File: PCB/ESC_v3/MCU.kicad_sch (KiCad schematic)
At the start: 44 parts, among them J10 Conn_01x01_Pin, J3 Conn_01x01_Pin, J4 Conn_01x01_Pin, J5 Conn_01x01_Pin, J6 Conn_01x01_Pin, J7 Conn_01x01_Pin, J8 Conn_01x01_Pin, J9 Conn_01x01_Pin, U5 STM32G431CBT6, Y2 24MHz

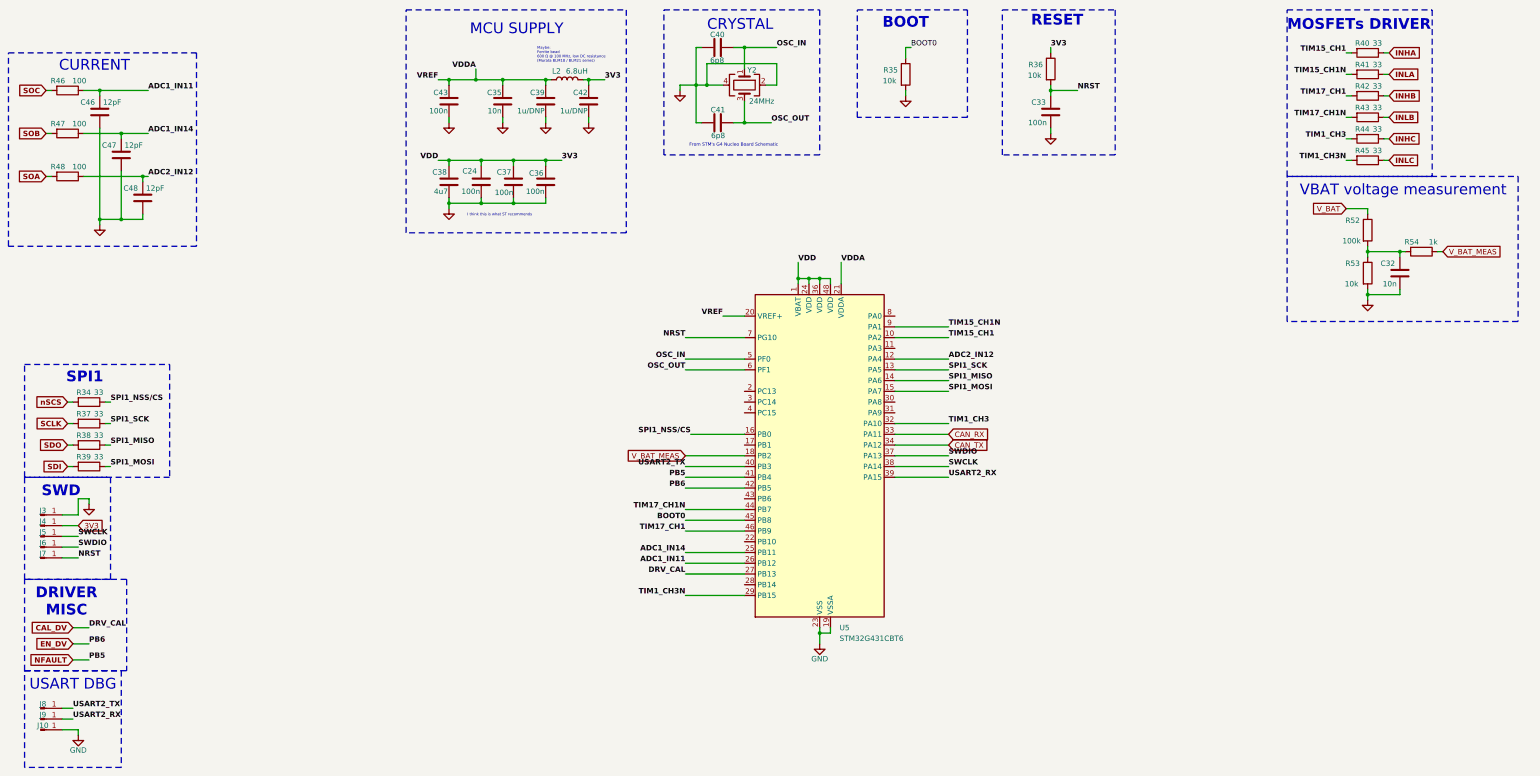
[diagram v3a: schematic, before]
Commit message: Reposition DRVR schematic elements
Adjust layout in PCB/ESC_v3/DRVR.kicad_sch: updated coordinates for rectangles, text labels, junctions, wires and pins to tidy and realign the driver schematic. Changes are graphical/coordinate-only (no netlist/electrical changes). Also touched project files (ESC_v3.*) and refreshed backup archives (deleted several older backups and added new snapshots).
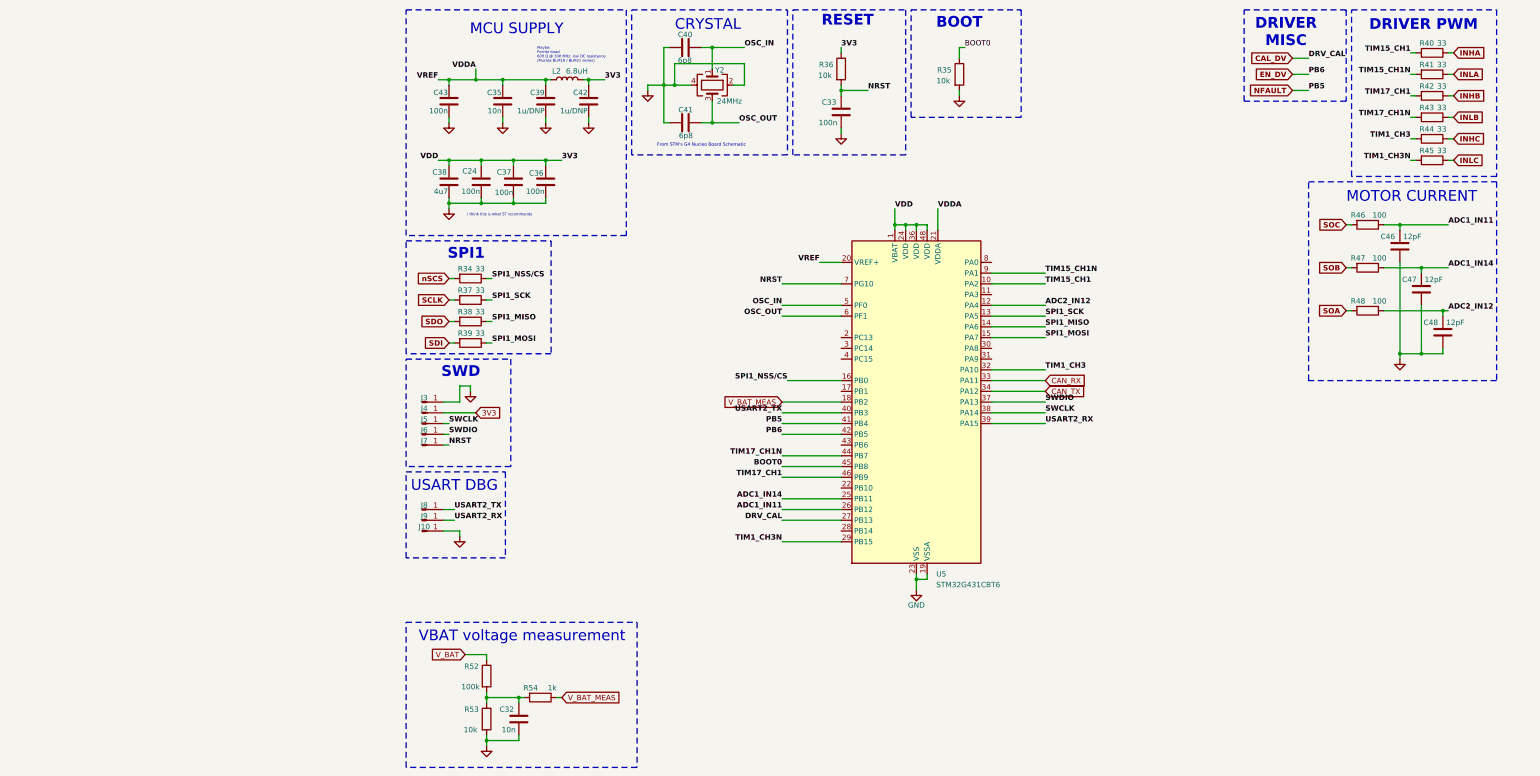
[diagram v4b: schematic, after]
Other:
- note added: "DRIVER PWM"
- note added: "MOTOR CURRENT"
- note removed: "CURRENT"
- note removed: "MOSFETs DRIVER"
- moved on the sheet: C32, C33, C40, C41, C46, C47, C48, J10, J3, J4, J5, J6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

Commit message: Update ESC_v3 schematics and PCB layout
Add net-tie symbol and +3V3/GND1 power symbols to DRVR schematic and reorganize schematic graphics (rectangles, text), junctions, and wires with updated coordinates/UUIDs. Also update top-level ESC_v3 schematic and MCU schematic along with PCB (.kicad_pcb) and panel (.kicad_prl) files. Remove several old backup zip files and add new backups for the ESC_v3 project.
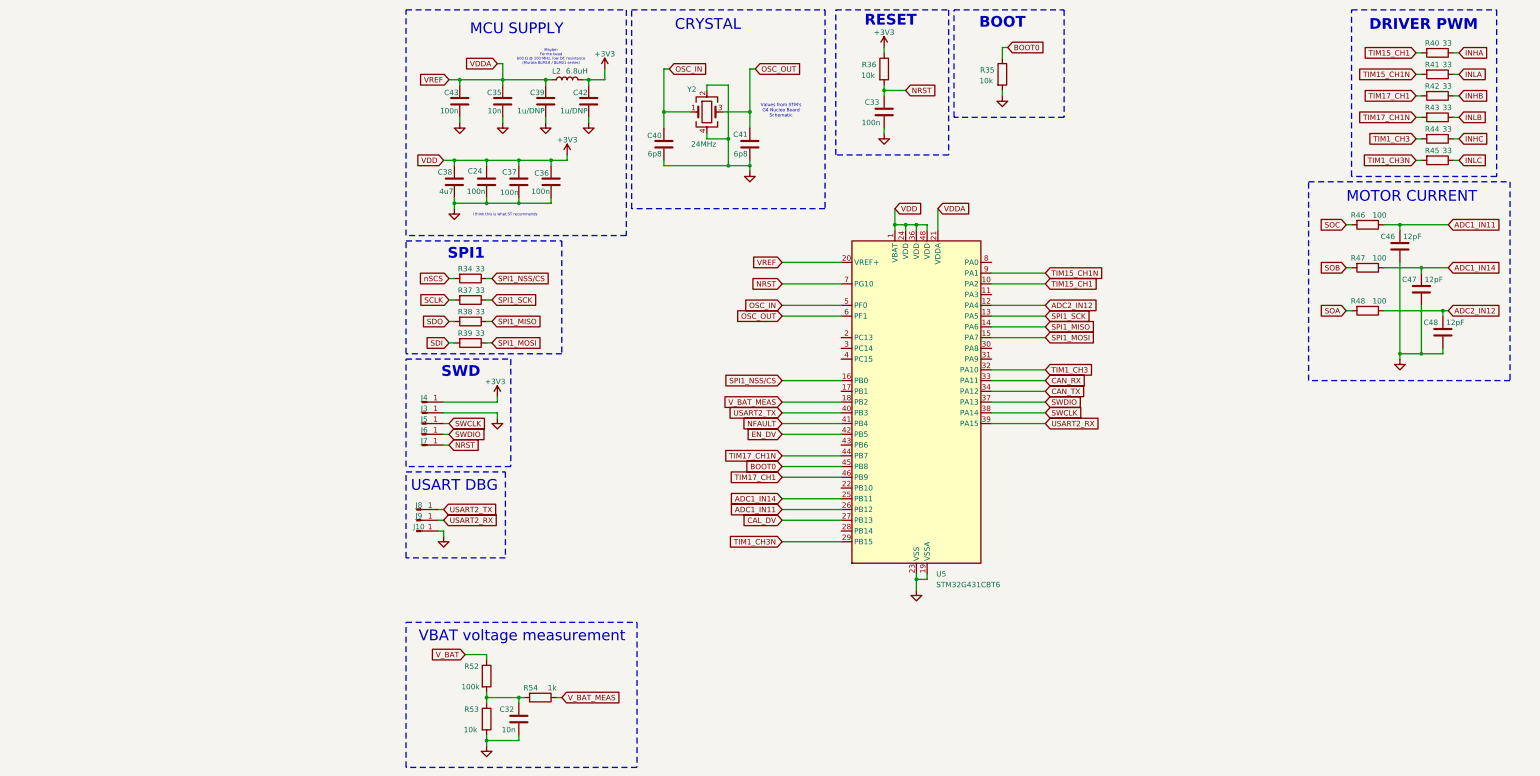
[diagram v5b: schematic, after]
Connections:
- net 3V3 renamed +3V3
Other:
- note added: "Values from STM's G4 Nucleo Board Schematic"
- note removed: "DRIVER MISC"
- note removed: "From STM's G4 Nucleo Board Schematic"
- moved on the sheet: C24, C33, C36, C37, C38, C40, C41, C43, J10, J3, J4, J8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

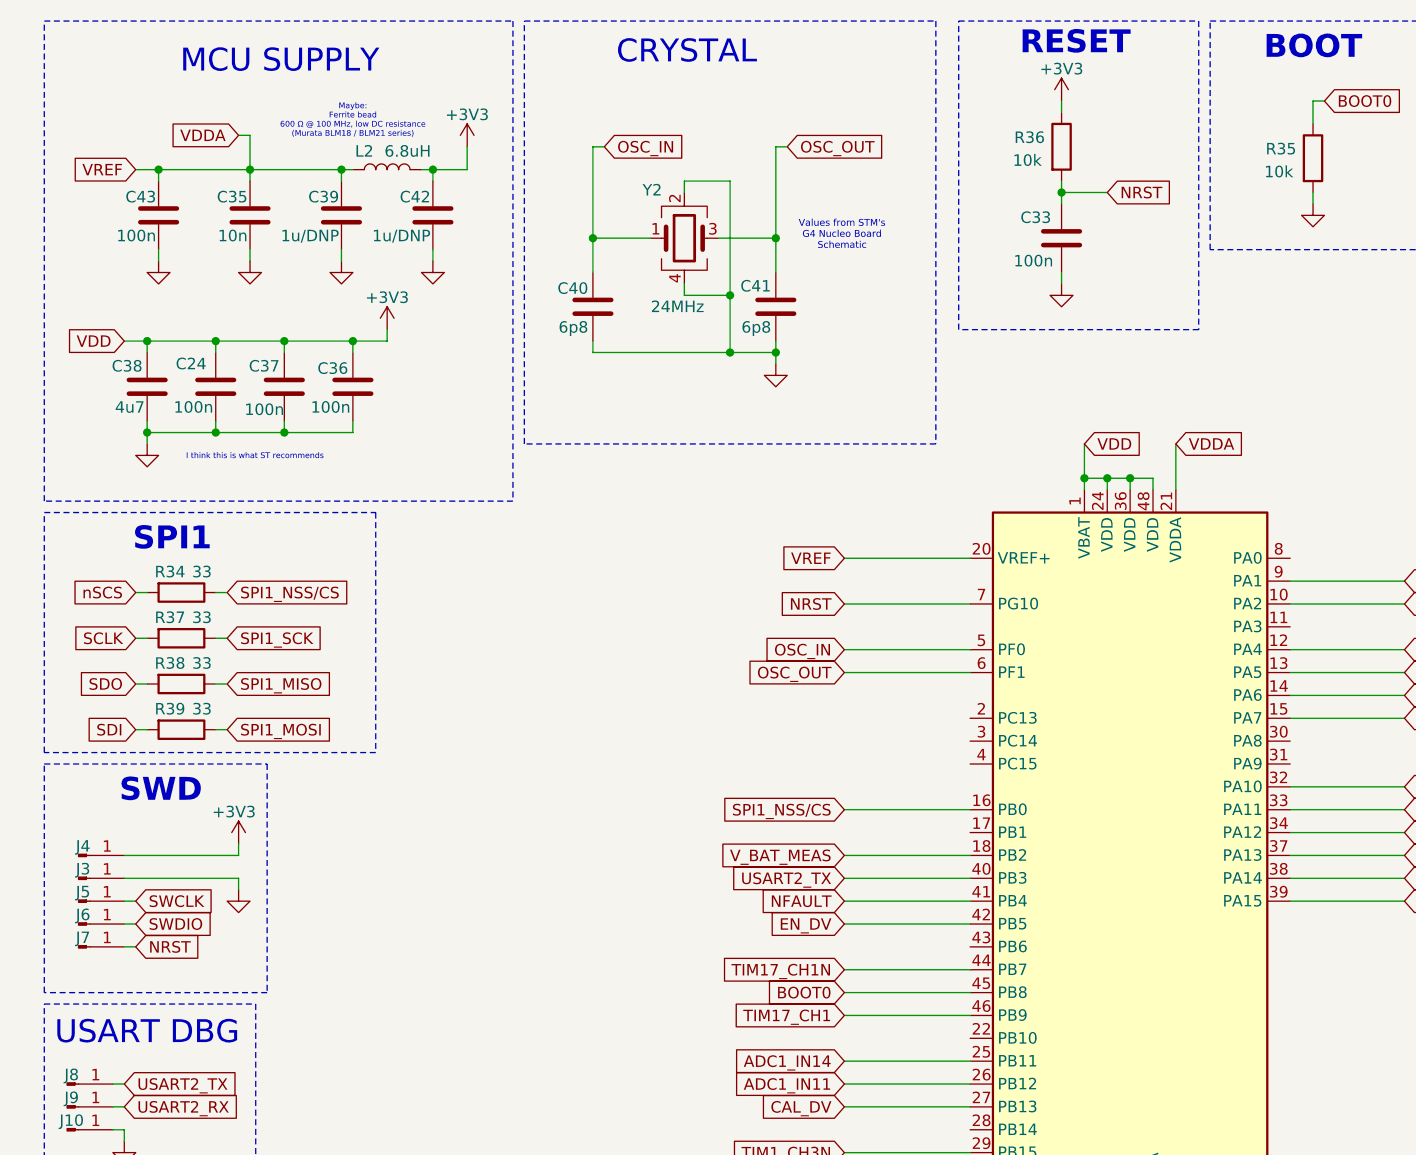
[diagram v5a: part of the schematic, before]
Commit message: Update DRVR schematic: relabels, wiring, net-ties
Refactor PCB/ESC_v3/DRVR.kicad_sch: cleaned up stray rectangles and comment text, repositioned many junctions and wires to fix connectivity, replaced/added global labels (reorganized SNA/SPA/SPB/SPC/SNB/SNC/etc.), and inserted NetTie symbols (NT1/NT3) with footprints to implement net ties. Updated symbol positions and UUIDs and removed obsolete schematic elements. Also touched top-level ESC_v3 files (ESC_v3.kicad_pcb, ESC_v3.kicad_prl, ESC_v3.kicad_sch, MCU.kicad_sch) and added/removed several backup archives.
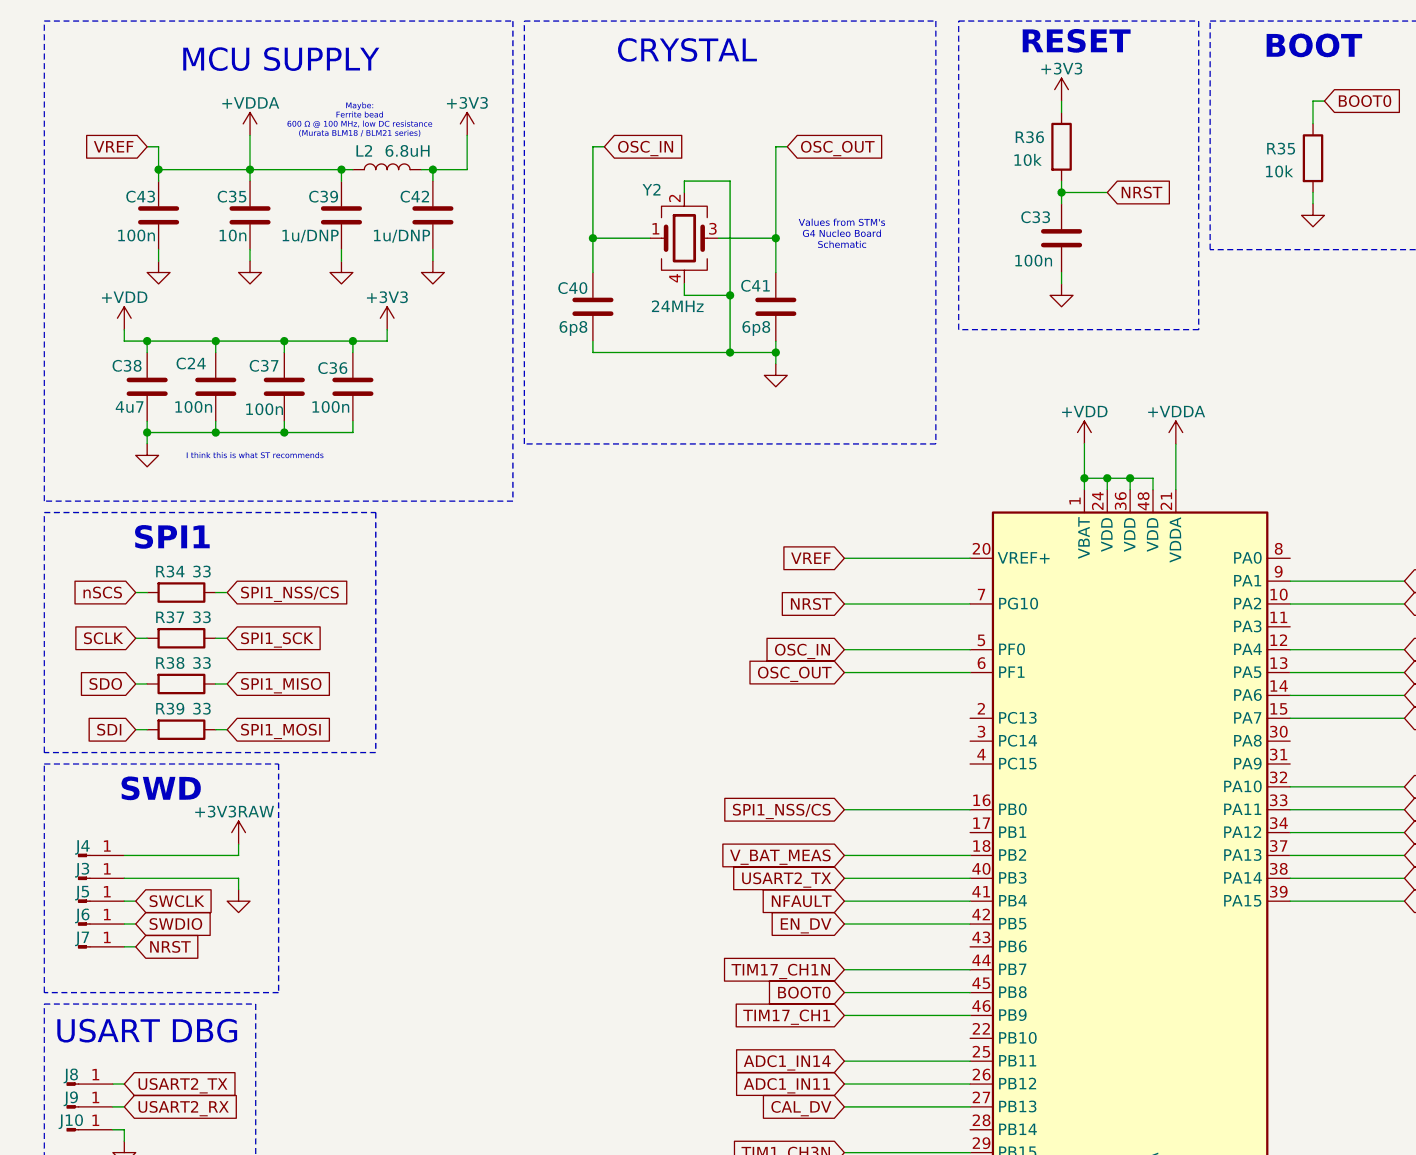
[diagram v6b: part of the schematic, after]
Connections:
- net +3V3: no longer J4.1 (Pin_1)
- net VDDA renamed +VDDA
- new net +3V3RAW: J4.1 (Pin_1)
